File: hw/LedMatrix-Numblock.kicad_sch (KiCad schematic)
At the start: 42 parts, among them Q2200 DTA114E, Q2201 DTA114E, Q2202 DTA114E, Q2203 DTA114E, Q2204 DTA114E, Q2205 DTA114E, Q2206 DTC114EE, Q2207 DTC114EE, Q2208 DTC114EE, Q2209 DTC114EE, Q2210 DTC114EE, Q2211 DTC114EE, Q2212 DTC114EE, Q2213 DTC114EE, Q2214 DTC114EE

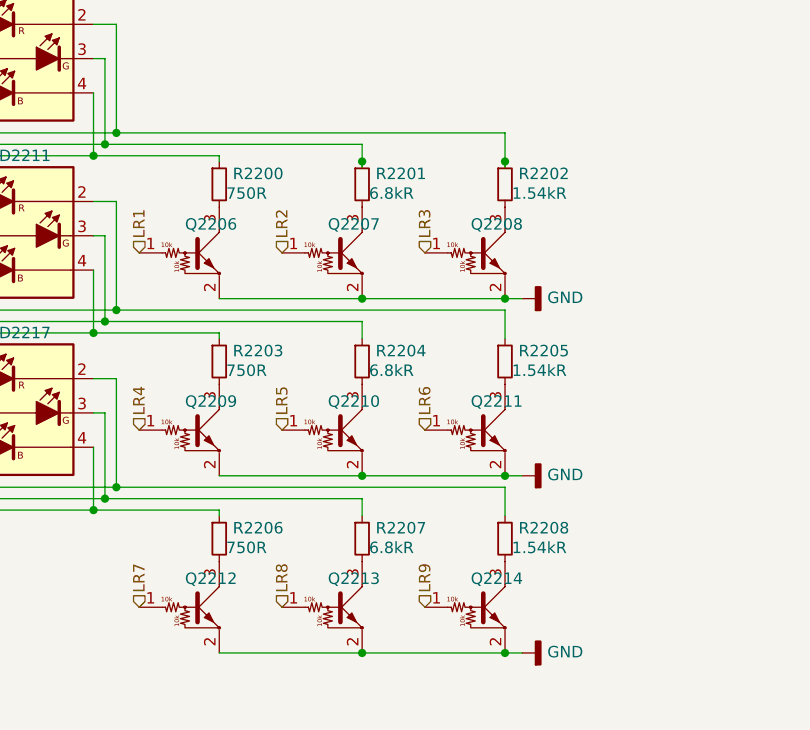
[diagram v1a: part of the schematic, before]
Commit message: Adjust LED matrix resistors.
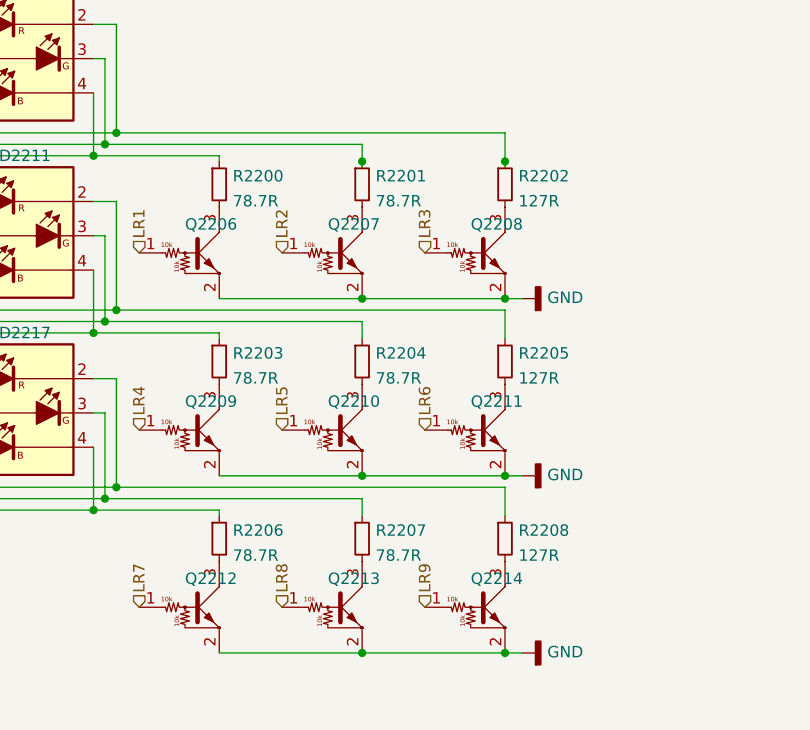
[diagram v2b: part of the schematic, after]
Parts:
- removed R2200, R2203, R2206: 750R, Keyboard:R_0402, symbol Keyboard:750R
- removed R2201, R2204, R2207: 6.8kR, Keyboard:R_0402, symbol Keyboard:6.8kR
- removed R2202, R2205, R2208: 1.54kR, Keyboard:R_0402, symbol Keyboard:1.54kR
- added R2200, R2201, R2203, R2204, R2206, R2207: 78.7R, Keyboard:R_0402, symbol Keyboard:78.7R
- added R2202, R2205, R2208: 127R, Keyboard:R_0402, symbol Keyboard:127R
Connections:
- net at D2200.2 (KR), D2201.2 (KR), D2202.2 (KR)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: now also R2202.1
- net at D2200.3 (KG), D2201.3 (KG), D2202.3 (KG)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: now also R2201.1
- net at D2200.4 (KB), D2201.4 (KB), D2202.4 (KB)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: now also R2200.1
- net at D2206.2 (KR), D2207.2 (KR), D2208.2 (KR)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: now also R2205.1
- net at D2206.3 (KG), D2207.3 (KG), D2208.3 (KG)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: now also R2204.1
- net at D2206.4 (KB), D2207.4 (KB), D2208.4 (KB)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: now also R2203.1
- net at D2212.2 (KR), D2213.2 (KR), D2214.2 (KR)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: now also R2208.1
- net at D2212.3 (KG), D2213.3 (KG), D2214.3 (KG)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: now also R2207.1
- net at D2212.4 (KB), D2213.4 (KB), D2214.4 (KB)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: now also R2206.1
- net at Q2208.3 (C): now also R2202.2
- net at Q2207.3 (C): now also R2201.2
- net at Q2206.3 (C): now also R2200.2
- net at Q2211.3 (C): now also R2205.2
- net at Q2212.3 (C): now also R2206.2
- net at Q2213.3 (C): now also R2207.2
- net at Q2214.3 (C): now also R2208.2
- net at Q2209.3 (C): now also R2203.2
- net at Q2210.3 (C): now also R2204.2
